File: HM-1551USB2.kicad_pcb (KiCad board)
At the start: 2 copper layers, 44 x 20.5 mm, 21 parts, among them Q1 IRLML6402, U1 USBLC6-2SC6, U2 FT232RL, U3 HM-MOD-UART

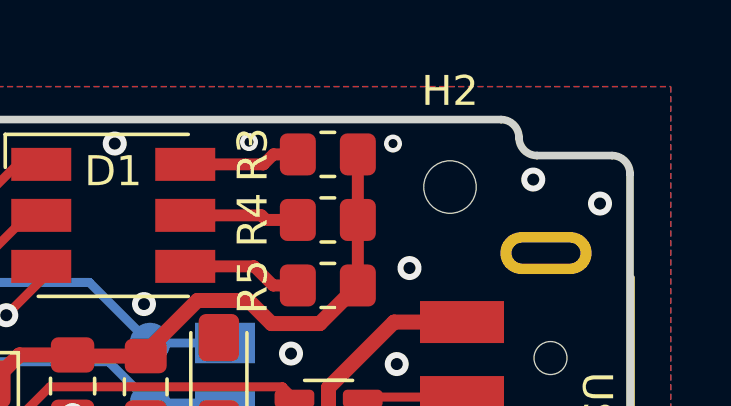
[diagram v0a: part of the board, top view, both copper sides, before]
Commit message: Update component properties and fill BOM
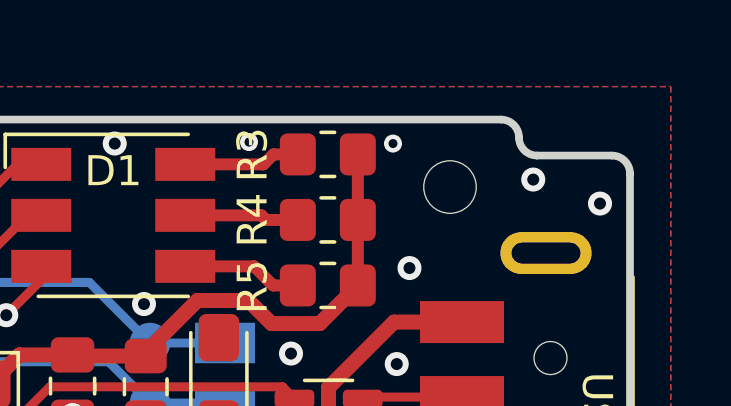
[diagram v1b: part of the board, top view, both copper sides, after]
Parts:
- C1: value 10nF -> 10µF
- C3: value 4.7uF -> 10µF
- C6: value 22uF -> 22µF
- L1: value Ferrite Bead -> 40R
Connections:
- USB1 pad 5: (no net) -> unconnected-(USB1-Pad5)
